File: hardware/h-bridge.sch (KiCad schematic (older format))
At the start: 83 parts, among them M1 MOUNTING_HOLE, M2 MOUNTING_HOLE, M3 MOUNTING_HOLE, M4 MOUNTING_HOLE, M5 MOUNTING_HOLE, M6 MOUNTING_HOLE, P10 CONN_01_BRK, P11 CONN_01_M+, P12 CONN_01_M-, P8 CONN_01_V+, P9 CONN_01_V-, Q10 PSMN021-100, Q3 IRFP4468, Q4 PSMN021-100, Q5 IRFP4468, Q6 IRFP4468, Q7 IRFP4468, Q8 IRFP4468, Q9 IRFP4468, U16 Si8045AA, U17 MIC4127, U18 MIC4127, U19 UCC27211, U20 Si8045AA, U6 UCC27211

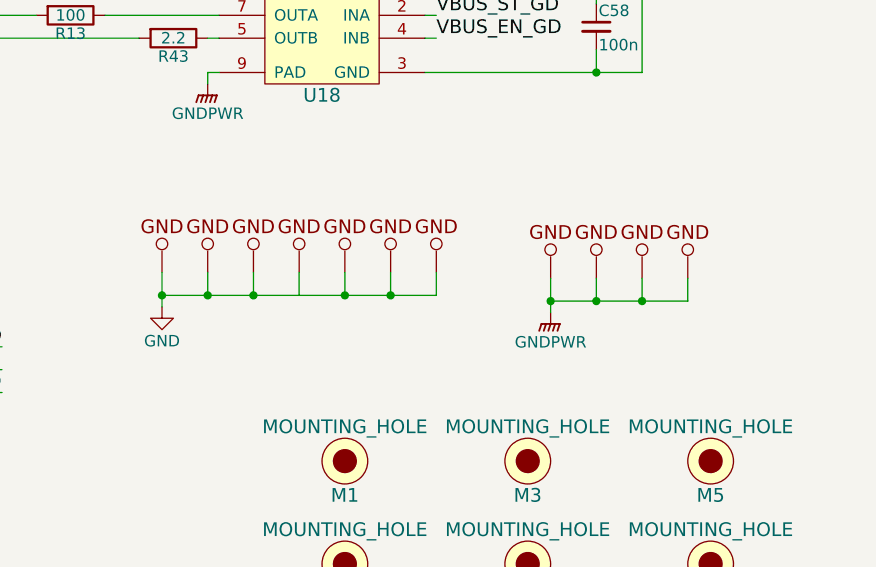
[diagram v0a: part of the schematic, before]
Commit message: Rev 0 board finished and submitted for manufacture
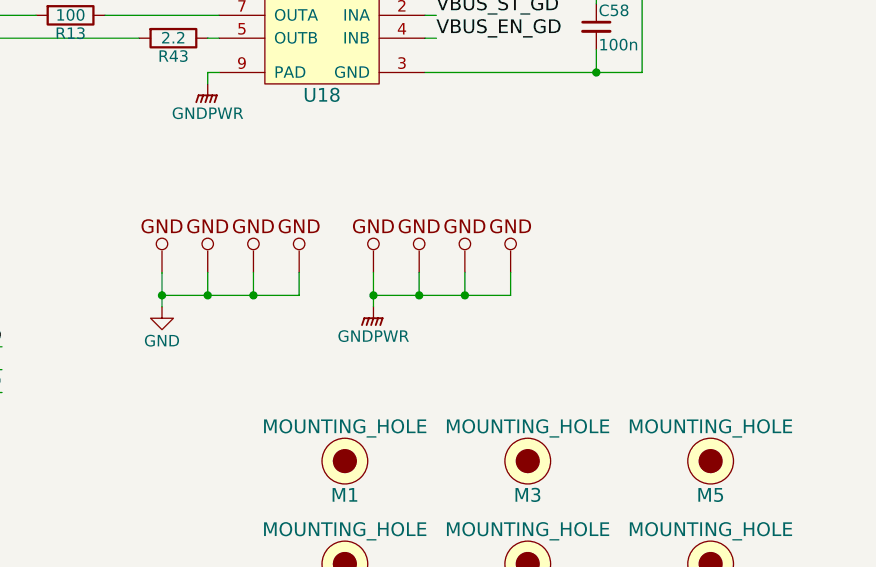
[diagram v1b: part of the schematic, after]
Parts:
- removed GND5, GND6, GND7: GND_POINT, 2kwMotorController:TEST_PAD_1.27mm, symbol GND_POINT
- GND1, GND2, GND3, GND4: footprint 2kwMotorController:TEST_PAD_1.27mm -> Pin_Headers:Pin_Header_Straight_1x01
- GND10, GND11, GND8, GND9: renamed from GND?; footprint 2kwMotorController:TEST_PAD_1.27mm -> Pin_Headers:Pin_Header_Straight_1x01
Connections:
- wire segments 207 -> 204

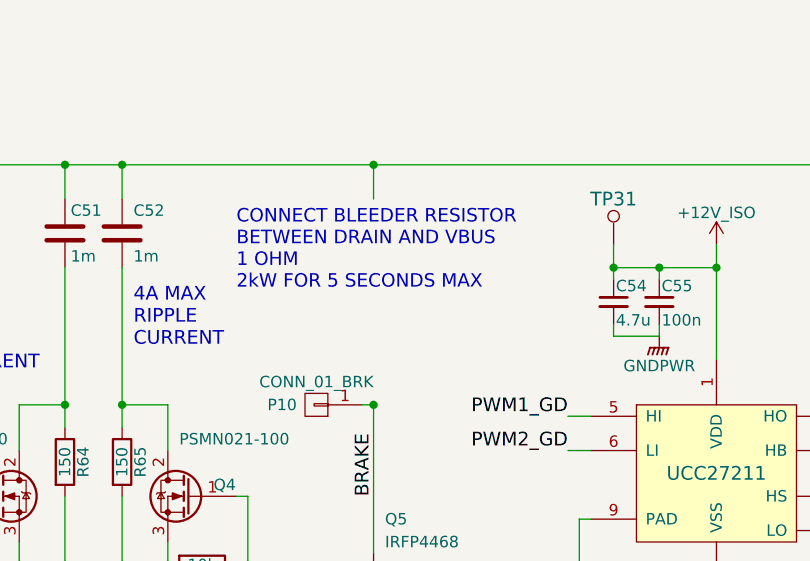
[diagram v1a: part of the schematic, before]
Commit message: Create and verify full Digikey BOM
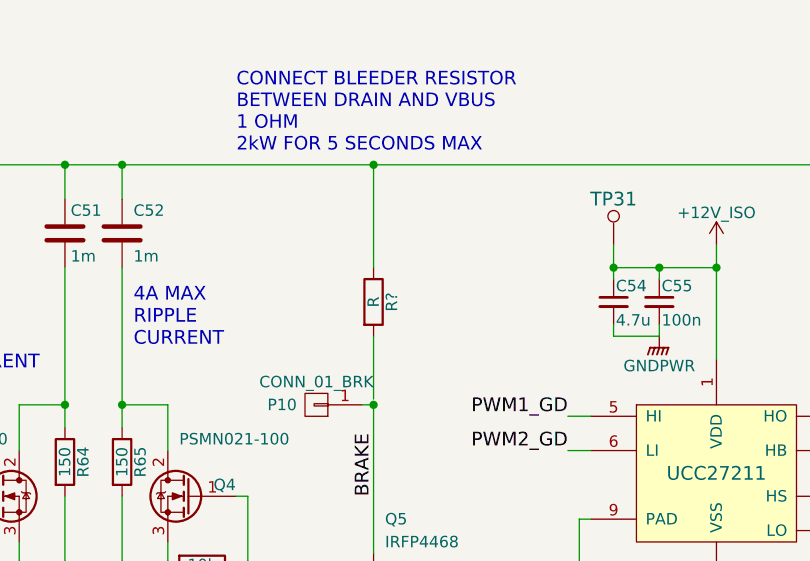
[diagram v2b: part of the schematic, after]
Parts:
- added R?: R, symbol R
- C50, C63: Voltage (none) -> 16V
- C51, C52, C56, C59, C61, C62, C64, C65, C66, C68: Voltage (none) -> 100V
- C53, C54, C55, C57, C58, C60, C67, C69, C70, C71, C80, C81: Voltage (none) -> 25V
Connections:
- net VBUS: now also R?.1
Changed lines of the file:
@@
 Text Notes 1700 950  2    79   ~ 16
 MOTOR BATTERY\n12V - 65V\nSCREW CONNECT
-Text Notes 3100 1650 0    59   ~ 0
+Text Notes 3100 1050 0    59   ~ 0
 CONNECT BLEEDER RESISTOR\nBETWEEN DRAIN AND VBUS\n1 OHM\n2kW FOR 5 SECONDS MAX
 Text HLabel 8050 5100 0    60   Input ~ 0
@@
 F 2 "Capacitors_SMD:C_0603" H 6150 2500 50  0001 C CNN
 F 3 "" H 6150 2500 50  0000 C CNN
+F 4 "25V" H 6150 2500 60  0001 C CNN "Voltage"
 	1    6150 2500
 	1    0    0    -1
@@
 F 2 "Capacitors_SMD:C_0603" H 4950 1700 50  0001 C CNN
 F 3 "" H 4950 1700 50  0000 C CNN
+F 4 "25V" H 4950 1700 60  0001 C CNN "Voltage"
 	1    4950 1700
 	1    0    0    -1
@@
 F 2 "Capacitors_SMD:C_0805" H 4750 1700 50  0001 C CNN
 F 3 "" H 4750 1700 50  0000 C CNN
+F 4 "25V" H 4750 1700 60  0001 C CNN "Voltage"
 	1    4750 1700
 	1    0    0    -1
@@
 F 2 "Capacitors_SMD:C_0603" H 9150 2500 50  0001 C CNN
 F 3 "" H 9150 2500 50  0000 C CNN
+F 4 "25V" H 9150 2500 60  0001 C CNN "Voltage"
 	1    9150 2500
 	-1   0    0    -1
@@
 F 2 "Capacitors_SMD:C_0603" H 10350 1700 50  0001 C CNN
 F 3 "" H 10350 1700 50  0000 C CNN
+F 4 "25V" H 10350 1700 60  0001 C CNN "Voltage"
 	1    10350 1700
 	-1   0    0    -1
@@
 F 2 "Capacitors_SMD:C_0805" H 10550 1700 50  0001 C CNN
 F 3 "" H 10550 1700 50  0000 C CNN
+F 4 "25V" H 10550 1700 60  0001 C CNN "Voltage"
 	1    10550 1700
 	-1   0    0    -1
@@
 F 1 "1m" H 2375 1300 50  0000 L CNN
 F 2 "2kwMotorController:Cap_Horizontal_D18_L36" H 2388 1250 50  0001 C CNN
-F 3 "" H 2350 1400 50  0000 C CNN
+F 3 "108CKS100MRY" H 2350 1400 50  0001 C CNN
+F 4 "100V" H 2350 1400 60  0001 C CNN "Voltage"
 	1    2350 1400
 	1    0    0    -1
@@
 F 1 "1m" H 2650 1500 50  0000 L CNN
 F 2 "2kwMotorController:Cap_Horizontal_D18_L36" H 2638 1250 50  0001 C CNN
-F 3 "" H 2600 1400 50  0000 C CNN
+F 3 "108CKS100MRY" H 2600 1400 50  0001 C CNN
+F 4 "100V" H 2600 1400 60  0001 C CNN "Voltage"
 	1    2600 1400
 	1    0    0    1
@@
 F 2 "Capacitors_SMD:C_0603" H 7900 4600 50  0001 C CNN
 F 3 "" H 7900 4600 50  0000 C CNN
+F 4 "16V" H 7900 4600 60  0001 C CNN "Voltage"
 	1    7900 4600
 	1    0    0    -1
@@
 F 2 "Capacitors_SMD:C_0603" H 9400 4600 50  0001 C CNN
 F 3 "" H 9400 4600 50  0000 C CNN
+F 4 "25V" H 9400 4600 60  0001 C CNN "Voltage"
 	1    9400 4600
 	1    0    0    -1
@@
 F 2 "Capacitors_SMD:C_0603" H 6100 4150 50  0001 C CNN
 F 3 "" H 6100 4150 50  0000 C CNN
+F 4 "25V" H 6100 4150 60  0001 C CNN "Voltage"
 	1    6100 4150
 	1    0    0    -1
@@
 F 2 "Capacitors_SMD:C_0603" H 6100 5000 50  0001 C CNN
 F 3 "" H 6100 5000 50  0000 C CNN
+F 4 "25V" H 6100 5000 60  0001 C CNN "Voltage"
 	1    6100 5000
 	1    0    0    -1
@@
 F 2 "Capacitors_SMD:C_1206" H 9488 1200 50  0001 C CNN
 F 3 "" H 9450 1350 50  0000 C CNN
+F 4 "100V" H 9450 1350 60  0001 C CNN "Voltage"
 	1    9450 1350
 	1    0    0    -1
@@
 F 2 "Capacitors_SMD:C_0603" H 1600 5900 50  0001 C CNN
 F 3 "" H 1600 5900 50  0000 C CNN
+F 4 "16V" H 1600 5900 60  0001 C CNN "Voltage"
 	1    1600 5900
 	1    0    0    -1
@@
 F 2 "Capacitors_SMD:C_0603" H 3100 5900 50  0001 C CNN
 F 3 "" H 3100 5900 50  0000 C CNN
+F 4 "25V" H 3100 5900 60  0001 C CNN "Voltage"
 	1    3100 5900
 	1    0    0    -1
@@
 F 2 "Capacitors_SMD:C_0603" H 8738 1200 50  0001 C CNN
 F 3 "" H 8700 1350 50  0000 C CNN
+F 4 "100V" H 8700 1350 60  0001 C CNN "Voltage"
 	1    8700 1350
 	1    0    0    -1
@@
 F 2 "Capacitors_SMD:C_0603" H 8988 1200 50  0001 C CNN
 F 3 "" H 8950 1350 50  0000 C CNN
+F 4 "100V" H 8950 1350 60  0001 C CNN "Voltage"
 	1    8950 1350
 	1    0    0    -1
@@
 F 2 "Capacitors_SMD:C_1206" H 9238 1200 50  0001 C CNN
 F 3 "" H 9200 1350 50  0000 C CNN
+F 4 "100V" H 9200 1350 60  0001 C CNN "Voltage"
 	1    9200 1350
 	1    0    0    -1
@@
 F 2 "Capacitors_SMD:C_0603" H 6588 1200 50  0001 C CNN
 F 3 "" H 6550 1350 50  0000 C CNN
+F 4 "100V" H 6550 1350 60  0001 C CNN "Voltage"
 	1    6550 1350
 	1    0    0    -1
@@
 F 2 "Capacitors_SMD:C_1206" H 5838 1200 50  0001 C CNN
 F 3 "" H 5800 1350 50  0000 C CNN
+F 4 "100V" H 5800 1350 60  0001 C CNN "Voltage"
 	1    5800 1350
 	1    0    0    -1
@@
 F 2 "Capacitors_SMD:C_1206" H 6088 1200 50  0001 C CNN
 F 3 "" H 6050 1350 50  0000 C CNN
+F 4 "100V" H 6050 1350 60  0001 C CNN "Voltage"
 	1    6050 1350
 	1    0    0    -1
@@
 F 2 "Capacitors_SMD:C_0603" H 6338 1200 50  0001 C CNN
 F 3 "" H 6300 1350 50  0000 C CNN
+F 4 "100V" H 6300 1350 60  0001 C CNN "Voltage"
 	1    6300 1350
 	1    0    0    -1
@@
 F 2 "Capacitors_SMD:C_0603" H 6350 2500 50  0001 C CNN
 F 3 "" H 6350 2500 50  0000 C CNN
+F 4 "25V" H 6350 2500 60  0001 C CNN "Voltage"
 	1    6350 2500
 	1    0    0    -1
@@
 F 2 "Capacitors_SMD:C_0603" H 8950 2500 50  0001 C CNN
 F 3 "" H 8950 2500 50  0000 C CNN
+F 4 "25V" H 8950 2500 60  0001 C CNN "Voltage"
 	1    8950 2500
 	-1   0    0    -1
@@
 	3700 2150 3700 2800
 Wire Wire Line
-	3700 1100 3700 1250
+	3700 1100 3700 1550
 Connection ~ 1050 3550
 Wire Wire Line
@@
 Wire Wire Line
 	4800 6175 4800 6075
+$Comp
+L R R?
+U 1 1 59D039D7
+P 3700 1700
+F 0 "R?" V 3780 1700 50  0000 C CNN
+F 1 "R" V 3700 1700 50  0000 C CNN
+F 2 "" V 3630 1700 50  0000 C CNN
+F 3 "" H 3700 1700 50  0000 C CNN
+	1    3700 1700
+	1    0    0    -1
+$EndComp
+Wire Wire Line
+	3700 2125 3700 1850
 $EndSCHEMATC

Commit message: Revised layout mostly complete
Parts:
- removed C51, C52: 1m, 2kwMotorController:Cap_Horizontal_D18_L36, symbol C
- removed GND10, GND11, GND3, GND4: GND_POINT, Pin_Headers:Pin_Header_Straight_1x01, symbol GND_POINT
- removed M1, M2, M3, M4, M5, M6: MOUNTING_HOLE, 2kwMotorController:M4-SCREW-HOLE, symbol MOUNTING_HOLE
- removed Q4: PSMN021-100, 2kwMotorController:SOT-669_LFPAK_ThermalVias-1, symbol Q_NMOS_GDS
- removed R39: 100, Resistors_SMD:R_0603, symbol R
- removed R41: 10k, Resistors_SMD:R_0603, symbol R
- removed R65: 150, 2kwMotorController:RESISTOR_FMP200, symbol R
- added C51, C52, C83, C84: 560u, 2kwMotorController:CP18, symbol CP
- gave numbers to parts that had none: 1
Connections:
- net labels removed: VBUS_ST_GATE_2
- wire segments 205 -> 197
- no-connect marks 1 -> 2
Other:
- moved on the sheet: Q10, R37, R64

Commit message: Update BOM
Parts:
- C54, C71: footprint Capacitors_SMD:C_0805 -> Capacitors_SMD:C_0603
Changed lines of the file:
@@
 F 0 "C54" H 4760 1770 50  0000 L CNN
 F 1 "4.7u" H 4760 1620 50  0000 L CNN
-F 2 "Capacitors_SMD:C_0805" H 4750 1700 50  0001 C CNN
+F 2 "Capacitors_SMD:C_0603" H 4750 1700 50  0001 C CNN
 F 3 "" H 4750 1700 50  0000 C CNN
 F 4 "25V" H 4750 1700 60  0001 C CNN "Voltage"
@@
 F 0 "C71" H 10560 1770 50  0000 L CNN
 F 1 "4.7u" H 10560 1620 50  0000 L CNN
-F 2 "Capacitors_SMD:C_0805" H 10550 1700 50  0001 C CNN
+F 2 "Capacitors_SMD:C_0603" H 10550 1700 50  0001 C CNN
 F 3 "" H 10550 1700 50  0000 C CNN
 F 4 "25V" H 10550 1700 60  0001 C CNN "Voltage"
